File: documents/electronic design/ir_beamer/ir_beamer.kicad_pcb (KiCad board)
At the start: 2 copper layers, 10 parts, among them P1 STM32F103_header, U1 74HC595D

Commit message: update pcb
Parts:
- removed P1: STM32F103_header, footprints:STM32F103C8T6_pin_header
- added U2: STM32F103HEADER, footprints:STM32F103_header_footprint, F.Cu at (19.3, 50.7)
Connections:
- net Net-(P1-PadG) renamed GND
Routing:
- net GND: track 78.5 -> 25.5 mm
- net +3.3: track 67.7 -> 17.1 mm

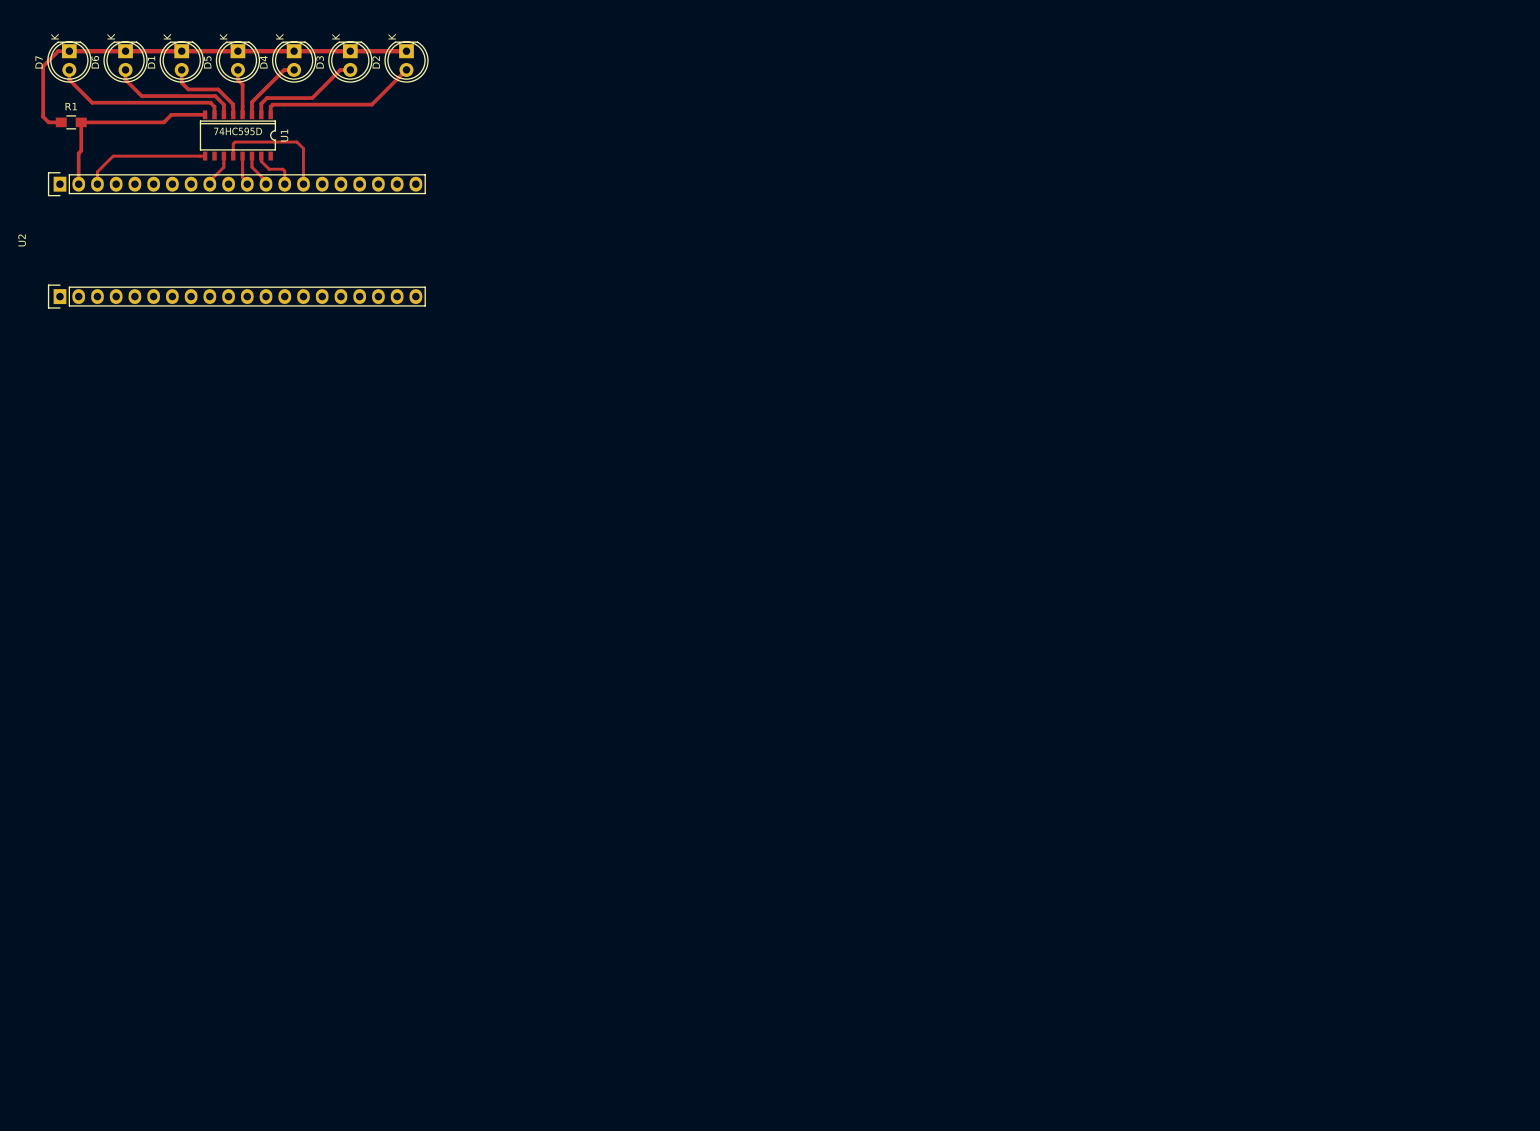
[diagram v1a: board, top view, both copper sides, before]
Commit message: fix pin numbers in ir_beamer
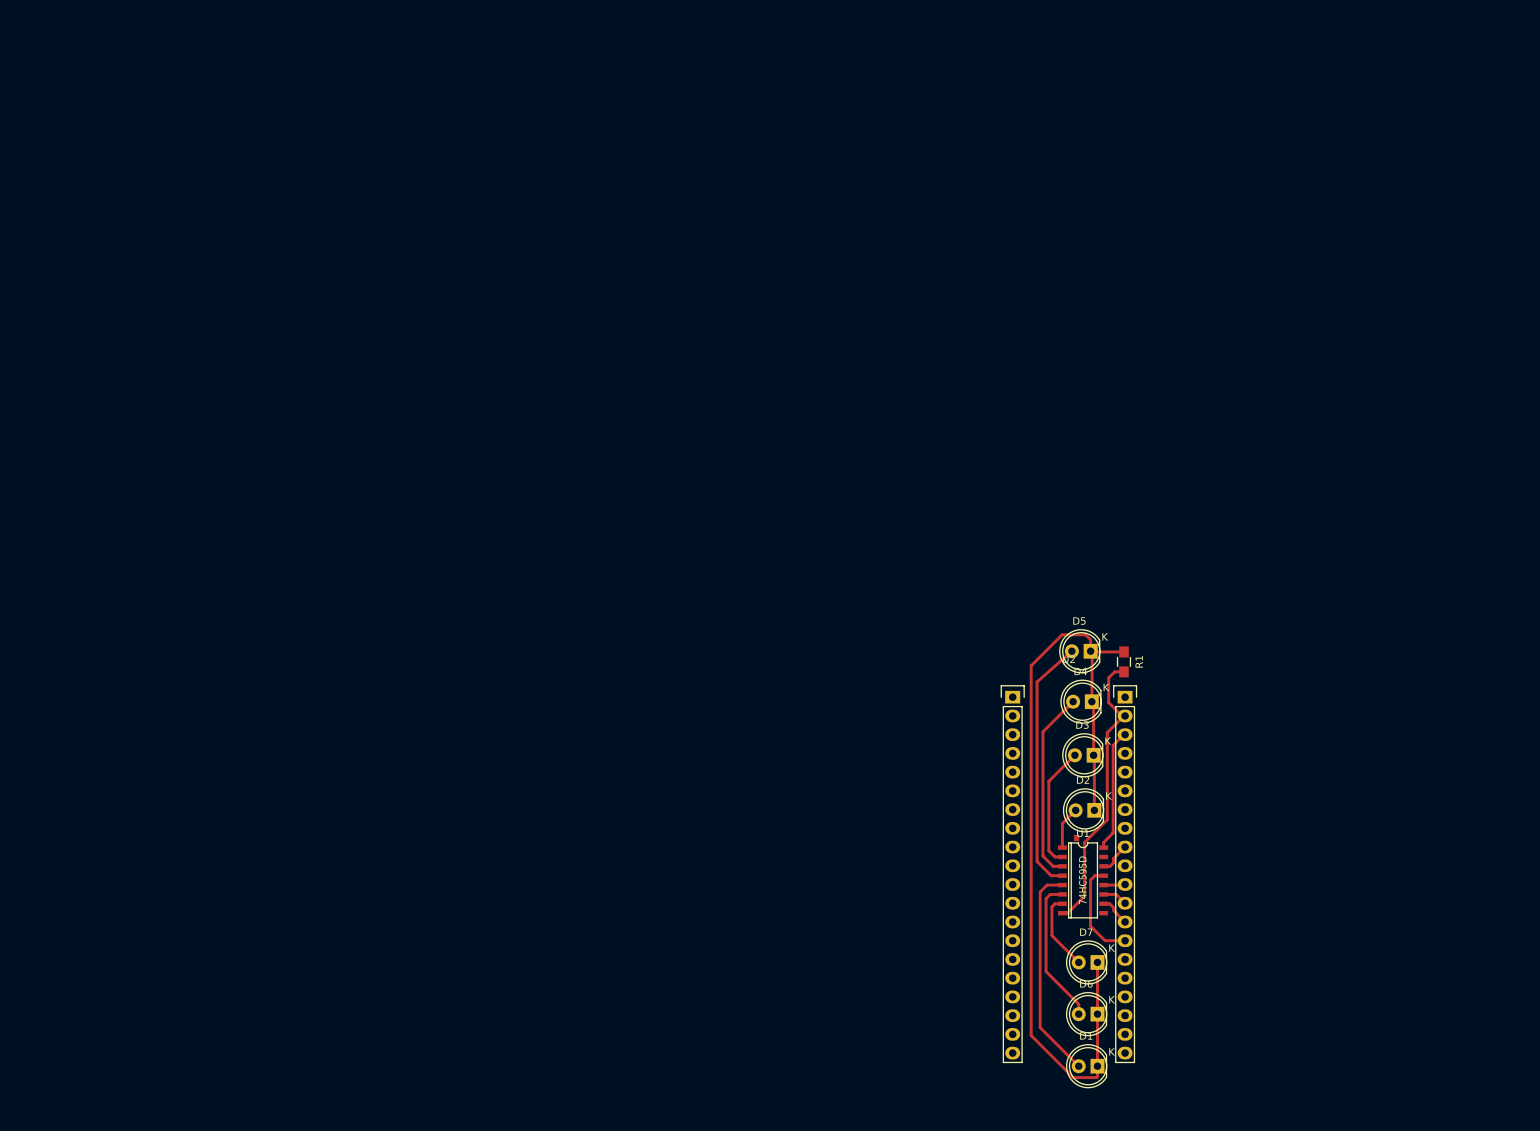
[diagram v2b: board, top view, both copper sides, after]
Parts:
- moved D7 186.3 mm to (160.0, 141.0), turned to 180 degrees
- moved D6 185.5 mm to (160.0, 148.0), turned to 180 degrees
- moved D1 185.4 mm to (160.0, 155.0), turned to 180 degrees
- moved R1 160.4 mm to (163.6, 100.2), turned to 270 degrees
- moved U1 152.8 mm to (158.0, 129.8), turned to 270 degrees
- moved D5 141.4 mm to (159.1, 98.8), turned to 180 degrees
- moved U2 140.2 mm to (148.5, 105.0), turned to 0 degrees
- moved D4 139.6 mm to (159.2, 105.6), turned to 180 degrees
- moved D2 138.9 mm to (159.6, 120.3), turned to 180 degrees
- moved D3 138.8 mm to (159.5, 112.9), turned to 180 degrees
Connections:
- U1 pad 10: Net-(U1-Pad10) -> MR_NOT
- U1 pad 11: SPI_MOSI -> ShiftReg_Expose
- U1 pad 12: OE_NOT -> SPI_SCK
- U1 pad 13: SPI_SCK -> OE_NOT
- U1 pad 14: ShiftReg_Expose -> SPI_MOSI
- U1 pad 15: MR_NOT -> Net-(U1-Pad15)
- U1 pad 16: Net-(U1-Pad16) -> +3V3
- U1 pad 9: +3.3 -> Net-(U1-Pad9)
- U2 pad 23: +3.3 -> +3V3
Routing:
- net Net-(D1-Pad1): track 59.7 -> 115.0 mm
- net Net-(D5-Pad2): track 6.35 -> 34.9 mm
- net Net-(D1-Pad2): track 11.4 -> 29.2 mm
- net +3.3: track 17.1 -> 0.00 mm
- net +3V3: track 0.00 -> 16.6 mm
- net Net-(D4-Pad2): track 9.24 -> 25.8 mm
- net Net-(D2-Pad2): track 21.6 -> 5.80 mm
- net GND: track 25.5 -> 39.5 mm
- net Net-(D7-Pad2): track 23.6 -> 10.6 mm
- net Net-(D6-Pad2): track 17.5 -> 19.9 mm
- net OE_NOT: track 16.2 -> 13.8 mm
- net ShiftReg_Expose: track 5.24 -> 3.40 mm
- net MR_NOT: track 5.95 -> 4.14 mm
- net Net-(D3-Pad2): track 15.5 -> 16.6 mm
- net SPI_SCK: track 3.81 -> 2.93 mm
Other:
- net class Default: trace_width 0.5 -> 0.4
- board text added: "."

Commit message: update pcb
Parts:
- removed R1: R, Resistors_SMD:R_0805_HandSoldering
- added T1: 2N7002K, footprints:SOT23, F.Cu at (169.3, 153.8)
- added T2: 2N7002K, footprints:SOT23, F.Cu at (176.9, 153.8)
- added T3: 2N7002K, footprints:SOT23, F.Cu at (184.5, 153.8)
- added T4: 2N7002K, footprints:SOT23, F.Cu at (192.1, 153.8)
- added T5: 2N7002K, footprints:SOT23, F.Cu at (199.8, 153.8)
- added T6: 2N7002K, footprints:SOT23, F.Cu at (207.4, 153.8)
- added T7: 2N7002K, footprints:SOT23, F.Cu at (215.0, 153.8)
- moved D5 71.5 mm to (199.8, 157.6), turned to 270 degrees
- moved D4 61.5 mm to (192.1, 157.6), turned to 270 degrees
- moved D7 57.5 mm to (215.0, 157.6), turned to 270 degrees
- moved D3 51.3 mm to (184.5, 157.6), turned to 270 degrees
- moved D6 48.4 mm to (207.4, 157.6), turned to 270 degrees
- moved U1 38.7 mm to (193.8, 144.8), turned to 0 degrees
- moved U2 38.7 mm to (186.7, 98.6)
- moved D2 38.5 mm to (169.3, 157.6), turned to 270 degrees
- moved D1 17.1 mm to (176.9, 157.6), turned to 270 degrees
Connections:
- D1 pad 2: Net-(D1-Pad2) -> IR_PWM
- D2 pad 1: Net-(D1-Pad1) -> Net-(D2-Pad1)
- D2 pad 2: Net-(D2-Pad2) -> IR_PWM
- D3 pad 1: Net-(D1-Pad1) -> Net-(D3-Pad1)
- D3 pad 2: Net-(D3-Pad2) -> IR_PWM
- D4 pad 1: Net-(D1-Pad1) -> Net-(D4-Pad1)
- D4 pad 2: Net-(D4-Pad2) -> IR_PWM
- D5 pad 1: Net-(D1-Pad1) -> Net-(D5-Pad1)
- D5 pad 2: Net-(D5-Pad2) -> IR_PWM
- D6 pad 1: Net-(D1-Pad1) -> Net-(D6-Pad1)
- D6 pad 2: Net-(D6-Pad2) -> IR_PWM
- D7 pad 1: Net-(D1-Pad1) -> Net-(D7-Pad1)
- D7 pad 2: Net-(D7-Pad2) -> IR_PWM
- U1 pad 1: Net-(D2-Pad2) -> IR_LED_1
- U1 pad 2: Net-(D3-Pad2) -> IR_LED_2
- U1 pad 3: Net-(D4-Pad2) -> IR_LED_3
- U1 pad 4: Net-(D5-Pad2) -> IR_LED_4
- U1 pad 5: Net-(D1-Pad2) -> IR_LED_5
- U1 pad 6: Net-(D6-Pad2) -> IR_LED_6
- U1 pad 7: Net-(D7-Pad2) -> IR_LED_7
- U2 pad 19: Net-(U2-Pad19) -> GND
- U2 pad 22: GND -> Net-(U2-Pad22)
- U2 pad 36: Net-(U2-Pad36) -> IR_PWM
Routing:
- net Net-(D1-Pad1): track 115.0 -> 2.80 mm
- net IR_PWM: track 0.00 -> 82.6 mm
- net GND: track 39.5 -> 89.3 mm
- net Net-(D5-Pad2): track 34.9 -> 0.00 mm
- net Net-(D1-Pad2): track 29.2 -> 0.00 mm
- net +3V3: track 16.6 -> 43.6 mm
- net Net-(D4-Pad2): track 25.8 -> 0.00 mm
- net SPI_MOSI: track 4.32 -> 27.4 mm
- net IR_LED_7: track 0.00 -> 21.8 mm
- net IR_LED_1: track 0.00 -> 21.6 mm
- net Net-(D6-Pad2): track 19.9 -> 0.00 mm
- net SPI_SCK: track 2.93 -> 21.2 mm
- net Net-(D3-Pad2): track 16.6 -> 0.00 mm
- net IR_LED_2: track 0.00 -> 16.3 mm
- net IR_LED_6: track 0.00 -> 15.8 mm
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
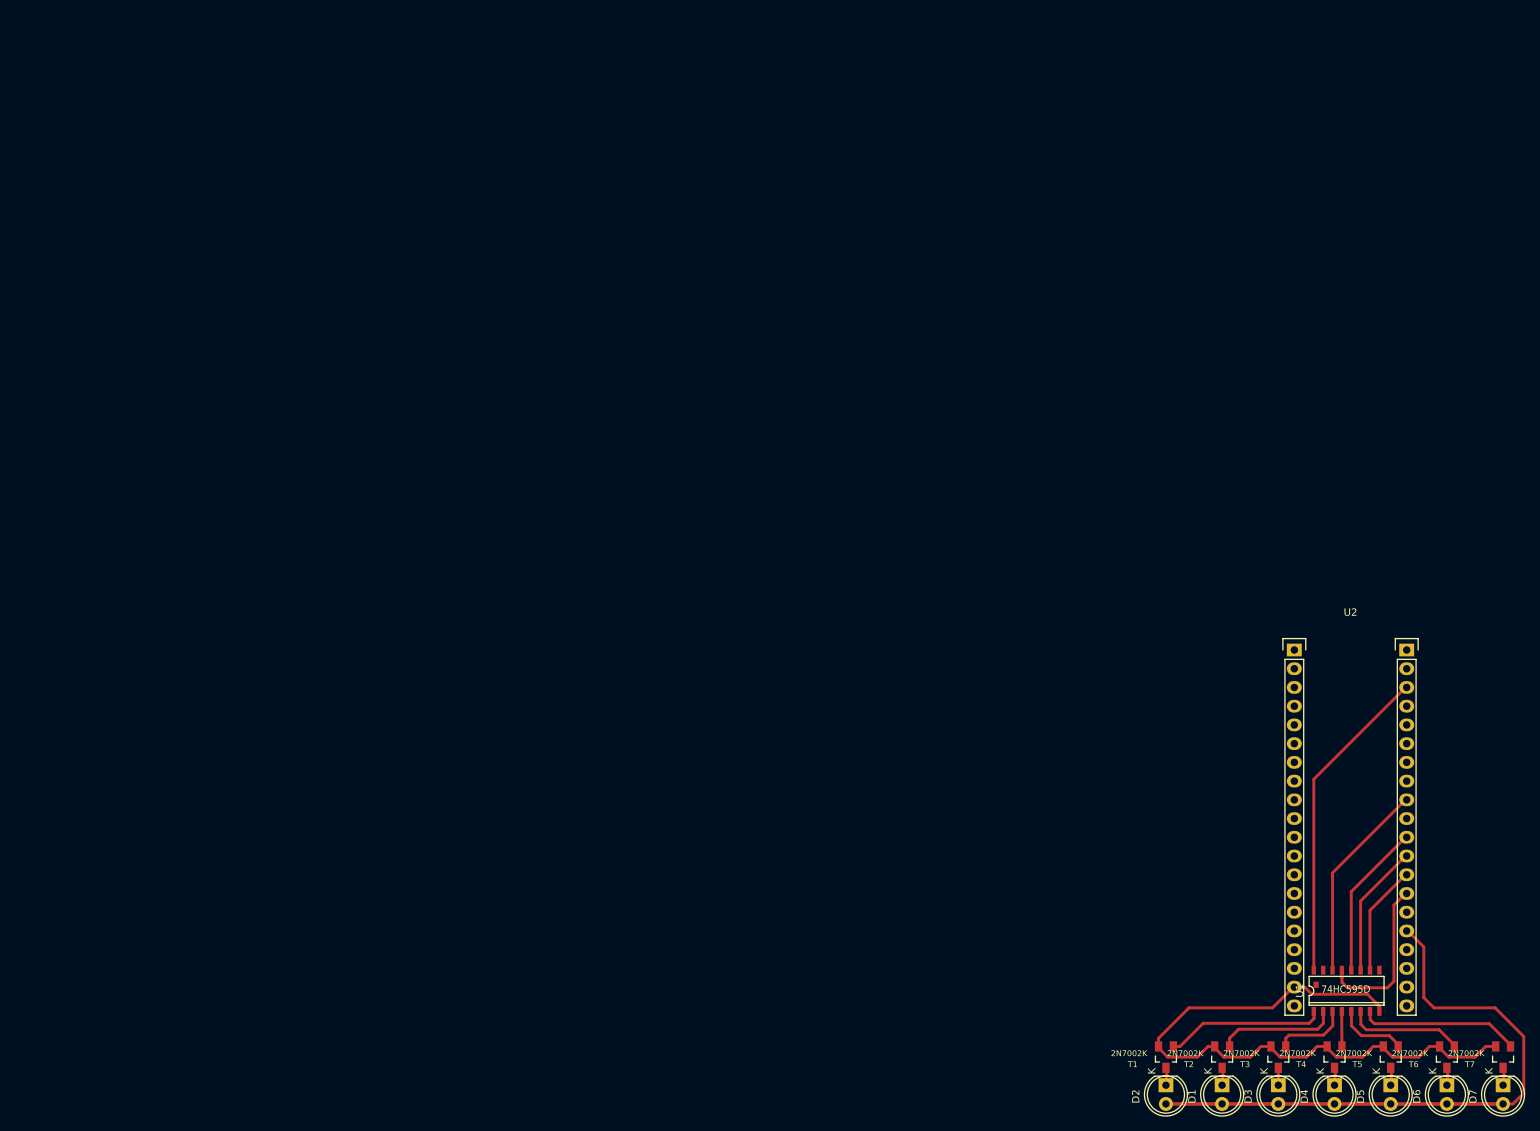
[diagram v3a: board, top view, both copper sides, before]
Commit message: make schematics for 10 IR led channels
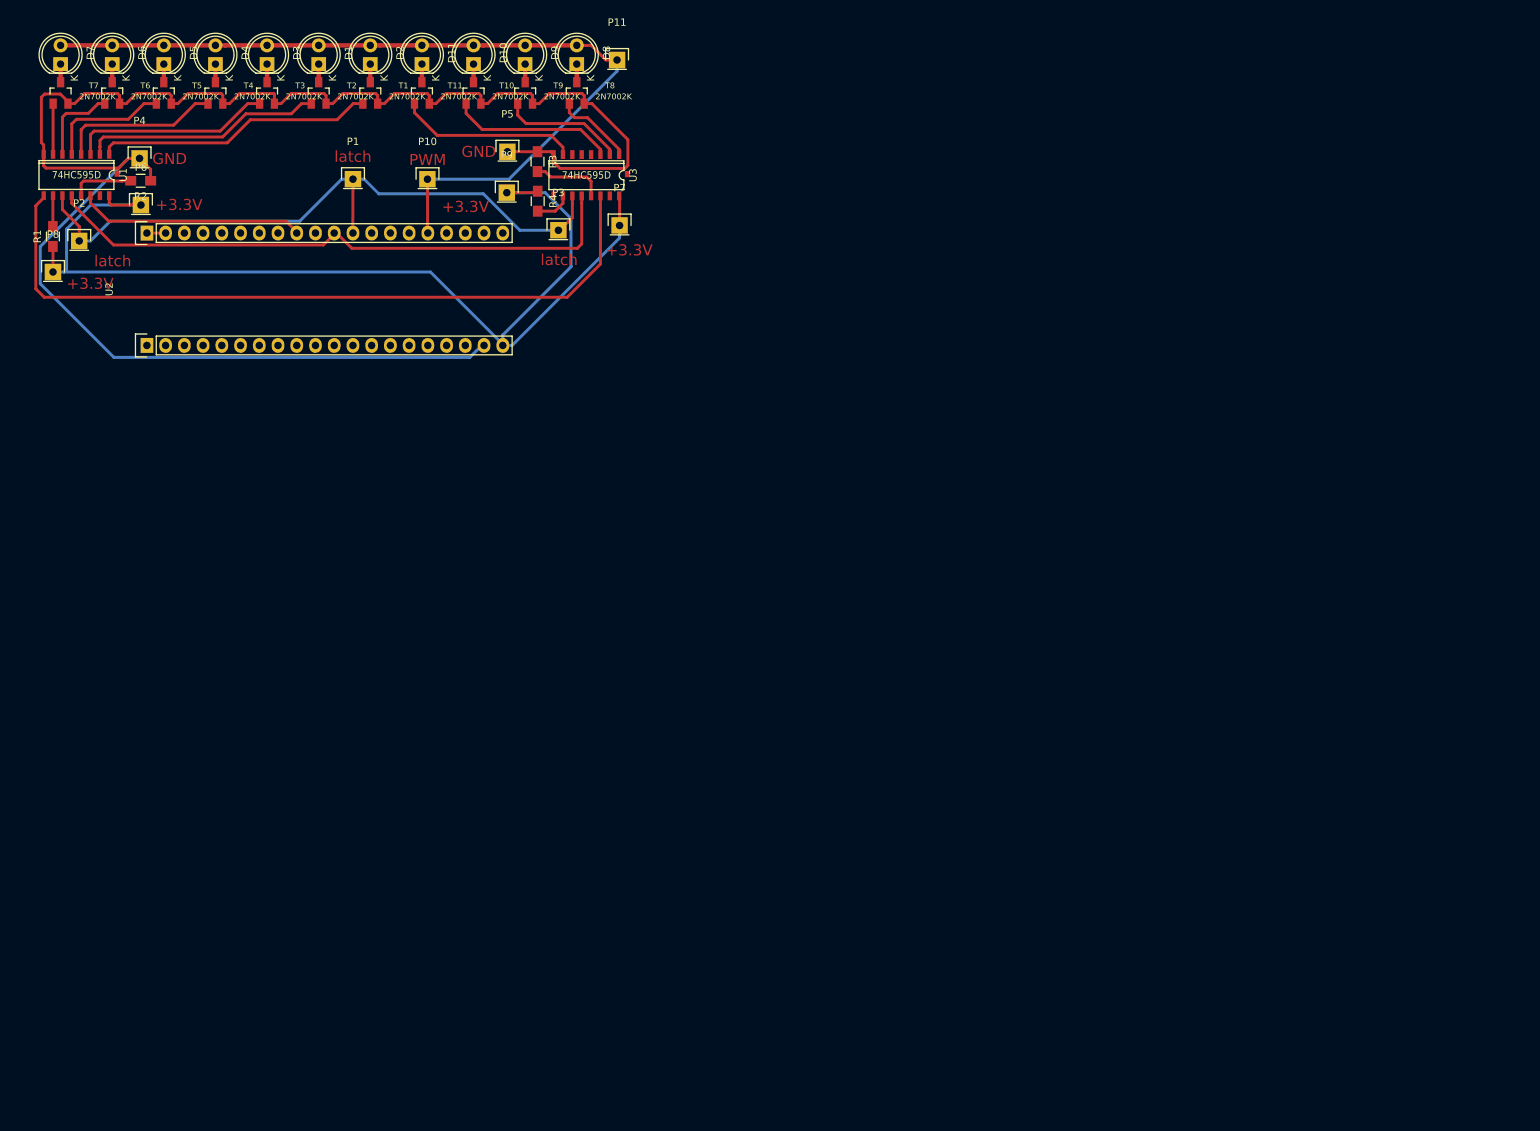
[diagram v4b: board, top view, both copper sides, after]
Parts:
- added D10: LED, LEDs:LED-5MM, F.Cu at (75.4, 19.1)
- added D11: LED, LEDs:LED-5MM, F.Cu at (68.4, 19.1)
- added D8: LED, LEDs:LED-5MM, F.Cu at (89.4, 19.1)
- added D9: LED, LEDs:LED-5MM, F.Cu at (82.4, 19.1)
- added P1: CONN_01X01, Pin_Headers:Pin_Header_Straight_1x01, F.Cu at (59.0, 34.8)
- added P10: CONN_01X01, Pin_Headers:Pin_Header_Straight_1x01, F.Cu at (69.1, 34.8)
- added P11: CONN_01X01, Pin_Headers:Pin_Header_Straight_1x01, F.Cu at (94.8, 18.6)
- added P2: CONN_01X01, Pin_Headers:Pin_Header_Straight_1x01, F.Cu at (21.9, 43.1)
- added P3: CONN_01X01, Pin_Headers:Pin_Header_Straight_1x01, F.Cu at (86.9, 41.7)
- added P4: CONN_01X01, Pin_Headers:Pin_Header_Straight_1x01, F.Cu at (30.1, 31.9)
- added P5: CONN_01X01, Pin_Headers:Pin_Header_Straight_1x01, F.Cu at (80.0, 31.0)
- added P6: CONN_01X01, Pin_Headers:Pin_Header_Straight_1x01, F.Cu at (30.3, 38.3)
- added P7: CONN_01X01, Pin_Headers:Pin_Header_Straight_1x01, F.Cu at (95.2, 41.0)
- added P8: CONN_01X01, Pin_Headers:Pin_Header_Straight_1x01, F.Cu at (18.4, 47.3)
- added P9: CONN_01X01, Pin_Headers:Pin_Header_Straight_1x01, F.Cu at (79.9, 36.6)
- added R1: R, Resistors_SMD:R_0805_HandSoldering, F.Cu at (18.3, 42.5)
- added R2: R, Resistors_SMD:R_0805_HandSoldering, F.Cu at (30.2, 35.0)
- added R3: R, Resistors_SMD:R_0805_HandSoldering, F.Cu at (84.1, 32.4)
- added R4: R, Resistors_SMD:R_0805_HandSoldering, F.Cu at (84.1, 37.7)
- added T10: 2N7002K, footprints:SOT23, F.Cu at (75.4, 23.1)
- added T11: 2N7002K, footprints:SOT23, F.Cu at (68.4, 23.1)
- added T8: 2N7002K, footprints:SOT23, F.Cu at (89.4, 23.1)
- added T9: 2N7002K, footprints:SOT23, F.Cu at (82.4, 23.1)
- added U3: 74HC595D, footprints:74HC595D_SO16, F.Cu at (90.7, 34.2)
- moved D7 239.7 mm to (19.4, 19.1), turned to 90 degrees
- moved T7 235.3 mm to (19.4, 23.1), turned to 0 degrees
- moved D6 227.9 mm to (26.4, 19.1), turned to 90 degrees
- moved T6 223.3 mm to (26.4, 23.1), turned to 0 degrees
- moved D5 216.5 mm to (33.4, 19.1), turned to 90 degrees
- moved T5 211.6 mm to (33.4, 23.1), turned to 0 degrees
- moved D4 205.4 mm to (40.4, 19.1), turned to 90 degrees
- moved U1 204.7 mm to (21.5, 34.2), turned to 180 degrees
- moved T4 200.3 mm to (40.4, 23.1), turned to 0 degrees
- moved D3 194.9 mm to (47.4, 19.1), turned to 90 degrees
- moved T3 189.5 mm to (47.4, 23.1), turned to 0 degrees
- moved D1 184.9 mm to (54.4, 19.1), turned to 90 degrees
- moved T2 179.2 mm to (54.4, 23.1), turned to 0 degrees
- moved D2 175.5 mm to (61.4, 19.1), turned to 90 degrees
- moved T1 169.5 mm to (61.4, 23.1), turned to 0 degrees
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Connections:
- net ShiftReg_Expose renamed Latch
- U1 pad 10: MR_NOT -> Net-(R1-Pad2)
- U1 pad 13: OE_NOT -> Net-(R2-Pad2)
- U2 pad 20: Net-(U2-Pad20) -> +3V3
- U2 pad 21: Net-(U2-Pad21) -> GND
- U2 pad 22: Net-(U2-Pad22) -> GND
- U2 pad 33: MR_NOT -> Net-(U2-Pad33)
- U2 pad 34: OE_NOT -> Net-(U2-Pad34)
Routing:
- net GND: track 89.3 -> 239.8 mm
- net +3V3: track 43.6 -> 154.8 mm
- net Net-(U1-Pad9): track 0.00 -> 101.2 mm
- net Latch: track 18.2 -> 91.2 mm
- net SPI_SCK: track 21.2 -> 81.1 mm
- net IR_PWM: track 82.6 -> 116.9 mm
- net IR_LED_DATA: track 0.00 -> 24.3 mm
- net IR_LED_10: track 0.00 -> 22.3 mm
- net OE_NOT: track 22.1 -> 0.00 mm
- net IR_LED_4: track 4.75 -> 22.0 mm
- net IR_LED_3: track 10.1 -> 27.3 mm
- net IR_LED_9: track 0.00 -> 16.7 mm
- net IR_LED_2: track 16.3 -> 32.6 mm
- net IR_LED_1: track 21.6 -> 37.8 mm
- net MR_NOT: track 15.1 -> 0.00 mm
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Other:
- board text added: "+3.3V"
- board text added: "GND"
- board text added: "PWM"
- board text added: "latch"
